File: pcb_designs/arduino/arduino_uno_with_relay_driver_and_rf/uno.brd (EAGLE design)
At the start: 157.2 x 94 mm, 53 parts, among them IC1 ATMEGA328, IC2 7805, Q1 12MHZ, T1 BC547, T2 BC547, T3 BC547, T4 BC547

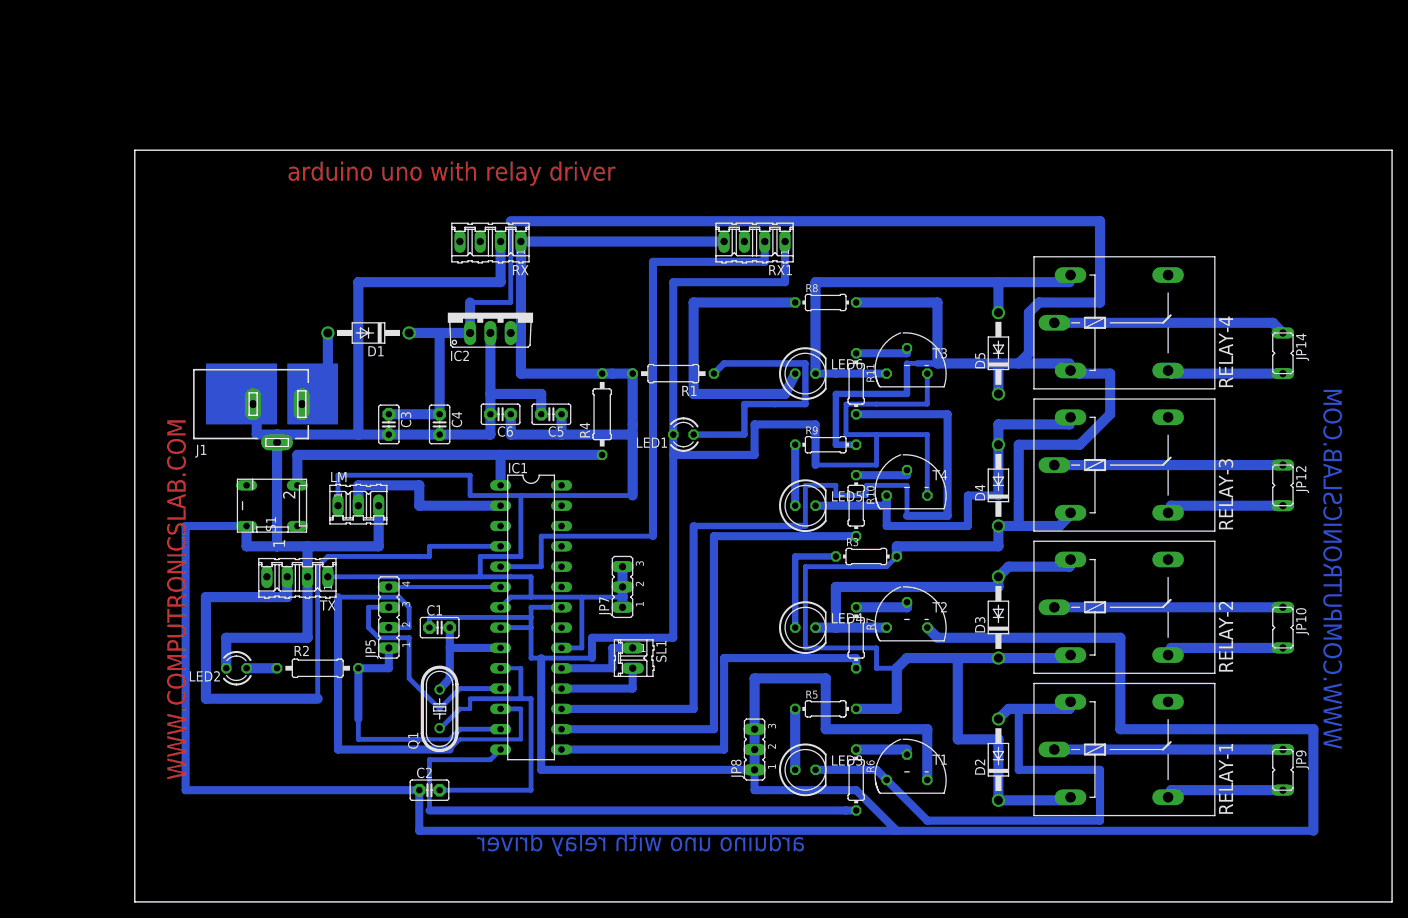
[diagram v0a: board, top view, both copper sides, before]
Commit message: 
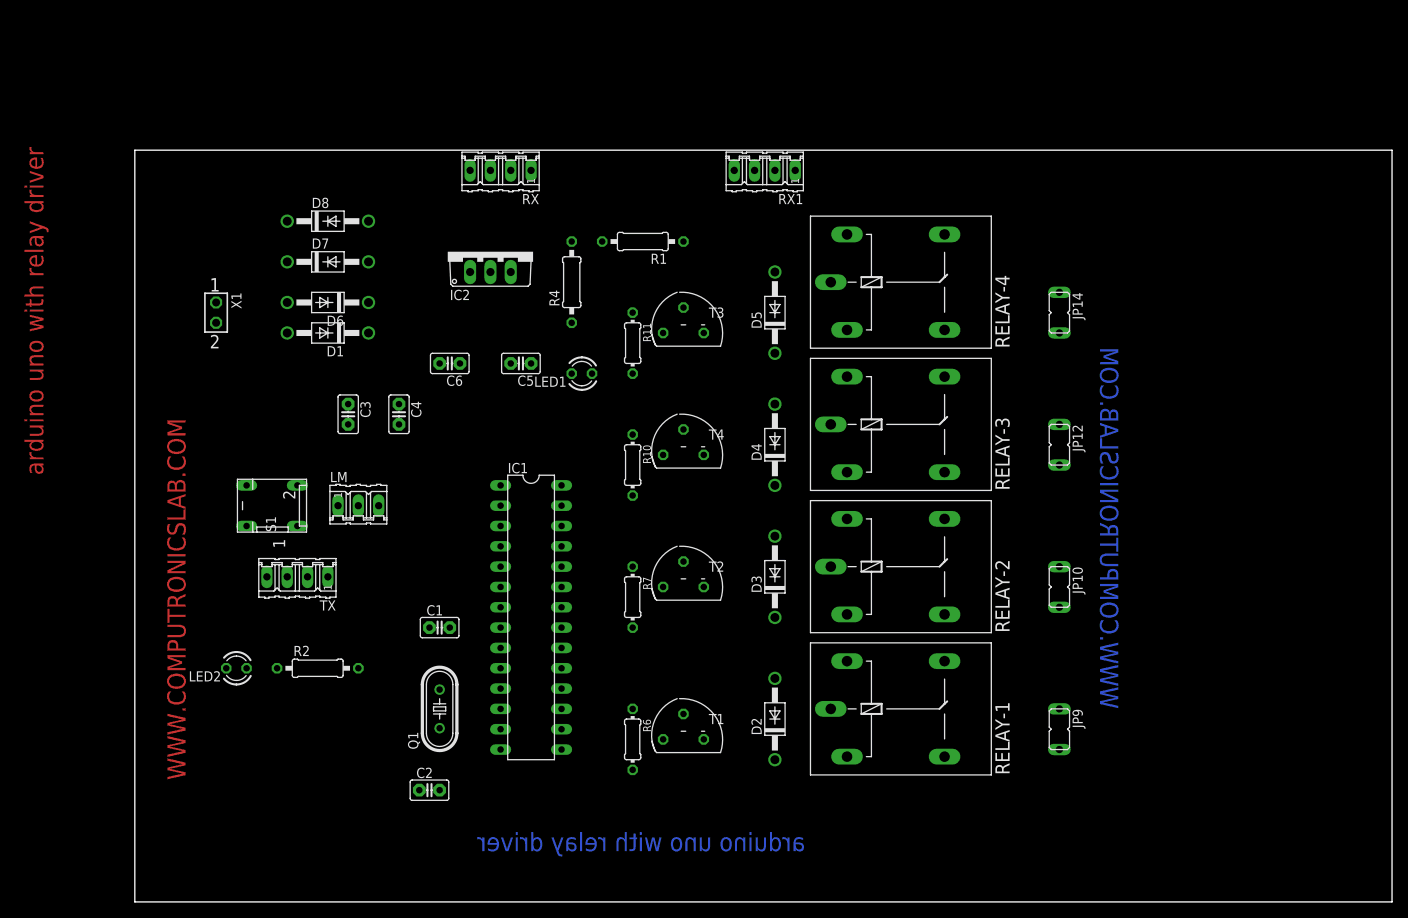
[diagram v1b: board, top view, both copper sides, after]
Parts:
- removed J1: (no value), con-jack:DCJ0303
- removed JP5: (no value), jumper:JP4
- removed JP7, JP8: (no value), jumper:JP2
- removed LED3, LED4, LED5, LED6: 5MM, led:LED5MM
- removed R3, R5, R8, R9: 1K, rcl:0204/7
- removed SL1: (no value), con-amp-quick:02P
- added D6, D7, D8: 1N4007, diode:DO41-10
- added X1: SSW-101-02-S-D, con-samtec:SSW-101-02-S-D
- C3: value 100UF -> 470uf
- moved D4 28.4 mm to (83.8, 66.0)
- moved D2 28.4 mm to (83.8, 31.8)
- moved D3 28.4 mm to (83.8, 49.5)
- moved D5 28.4 mm to (83.8, 82.5)
- moved RELAY-1 28.4 mm to (100.3, 33.0)
- moved RELAY-2 28.4 mm to (100.3, 50.8)
- moved RELAY-3 28.4 mm to (100.3, 68.6)
- moved RELAY-4 28.4 mm to (100.3, 86.4)
- moved JP12 28.4 mm to (119.4, 66.0)
- moved JP9 28.4 mm to (119.4, 30.5)
- moved R6 28.4 mm to (66.0, 29.2)
- moved R7 28.4 mm to (66.0, 47.0)
- moved T1 28.4 mm to (72.4, 30.5)
- moved T4 28.4 mm to (72.4, 66.0)
- moved JP10 28.4 mm to (119.4, 48.3)
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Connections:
- removed net N$18: IC1.6, JP5.4
- removed net N$19: IC1.12, JP5.2
- removed net N$20: IC1.11, JP5.3
- removed net N$27: IC1.19, SL1.1
- removed net N$3: D1.A, J1.1
- removed net N$33: LED3.A, R5.1
- removed net N$34: LED4.A, R3.1
- removed net N$47: LED5.A, R9.1
- removed net N$48: LED6.A, R8.1
- removed net N$5: IC1.18, SL1.2
- new net N$10: D6.A, D7.C, X1.1
- new net N$12: D1.A, D8.C, X1.2
- net N$21: no longer JP5.1
- net N$28: no longer LED3.K
- net N$4: no longer JP7.1, JP7.2, JP7.3
- net N$42: no longer LED4.K
- net N$43: no longer LED5.K
- net N$55: now also D7.A, D8.A; no longer J1.2, J1.3, JP8.1, JP8.2, JP8.3
- net N$58: no longer LED6.K
- net N$7: now also D6.C; no longer R3.2, R5.2, R8.2, R9.2
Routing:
- net N$55: track 714.3 -> 0.00 mm
- net N$7: track 370.7 -> 0.00 mm
- net N$4: track 210.1 -> 0.00 mm
- net N$57: track 106.7 -> 0.00 mm
- net N$11: track 80.5 -> 0.00 mm
- net N$9: track 73.7 -> 0.00 mm
- net N$28: track 72.6 -> 0.00 mm
- net N$41: track 69.1 -> 0.00 mm
- net N$19: track 63.3 -> 0.00 mm
- net N$56: track 61.0 -> 0.00 mm
- net N$58: track 56.8 -> 0.00 mm
- net N$43: track 50.4 -> 0.00 mm
- net N$59: track 49.5 -> 0.00 mm
- net N$42: track 45.9 -> 0.00 mm
- net N$31: track 45.7 -> 0.00 mm
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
